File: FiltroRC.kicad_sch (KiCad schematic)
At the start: 2 parts

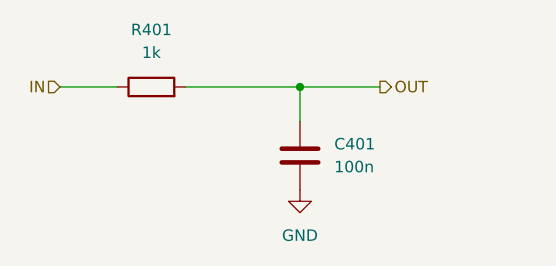
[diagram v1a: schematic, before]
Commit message: Microcontrolador: STM32G031K8T6, SWD, conector E/S y 3 filtros RC (huellas y MPN)
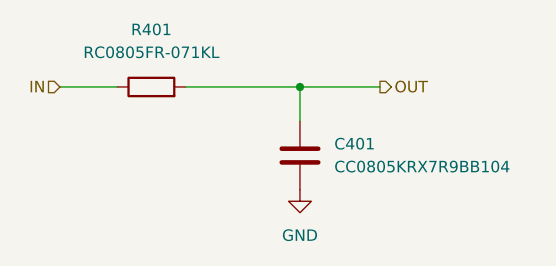
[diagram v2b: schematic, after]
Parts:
- C401: value 100n -> CC0805KRX7R9BB104; footprint (none) -> Capacitor_SMD:C_0805_2012Metric_Pad1.18x1.45mm_HandSolder
- R401: value 1k -> RC0805FR-071KL; footprint (none) -> Resistor_SMD:R_0805_2012Metric_Pad1.20x1.40mm_HandSolder
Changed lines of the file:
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@@
 			)
 		)
-		(property "Value" "100n"
+		(property "Value" "CC0805KRX7R9BB104"
 			(at 109.22 81.2799 0)
 			(show_name no)
@@
 			)
 		)
-		(property "Footprint" ""
+		(property "Footprint" "Capacitor_SMD:C_0805_2012Metric_Pad1.18x1.45mm_HandSolder"
 			(at 104.4448 76.2 0)
 			(hide yes)
@@
 			)
 		)
-		(property "Value" "1k"
+		(property "Value" "RC0805FR-071KL"
 			(at 88.9 68.58 90)
 			(show_name no)
@@
 			)
 		)
-		(property "Footprint" ""
+		(property "Footprint" "Resistor_SMD:R_0805_2012Metric_Pad1.20x1.40mm_HandSolder"
 			(at 88.9 74.168 90)
 			(hide yes)

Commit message: Correcciones: huella C202, conectores J301/J302, SWD al MCU, MPN en su campo y BOM
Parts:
- C401: MPN (none) -> CC0805KRX7R9BB104; Manufacturer (none) -> YAGEO
- R401: MPN (none) -> RC0805FR-071KL; Manufacturer (none) -> YAGEO
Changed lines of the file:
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@@
 			)
 		)
-		(property "MPN" ""
+		(property "MPN" "CC0805KRX7R9BB104"
 			(at 105.41 80.01 0)
 			(hide yes)
@@
 			)
 		)
-		(property "Manufacturer" ""
+		(property "Manufacturer" "YAGEO"
 			(at 105.41 80.01 0)
 			(hide yes)
@@
 			)
 		)
-		(property "MPN" ""
+		(property "MPN" "RC0805FR-071KL"
 			(at 88.9 72.39 90)
 			(hide yes)
@@
 			)
 		)
-		(property "Manufacturer" ""
+		(property "Manufacturer" "YAGEO"
 			(at 88.9 72.39 90)
 			(hide yes)

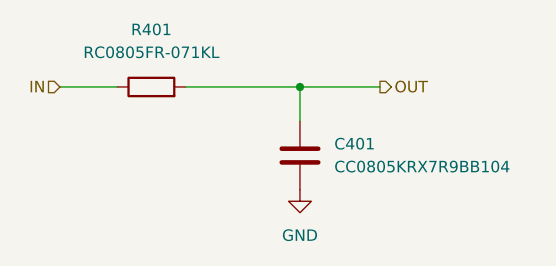
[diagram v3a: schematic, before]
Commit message: Valores eléctricos en Value y BOM actualizada
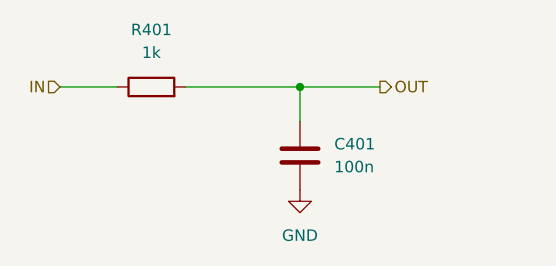
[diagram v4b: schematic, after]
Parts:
- C401: value CC0805KRX7R9BB104 -> 100n
- R401: value RC0805FR-071KL -> 1k
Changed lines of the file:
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@@
 			)
 		)
-		(property "Value" "CC0805KRX7R9BB104"
+		(property "Value" "100n"
 			(at 109.22 81.2799 0)
 			(show_name no)
@@
 			)
 		)
-		(property "Value" "RC0805FR-071KL"
+		(property "Value" "1k"
 			(at 88.9 68.58 90)
 			(show_name no)
